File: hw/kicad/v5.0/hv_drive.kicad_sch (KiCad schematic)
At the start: 27 parts, among them P6 CONN_01X02, P8 CONN_01X03, U12 IKCM30F60GAXKMA1

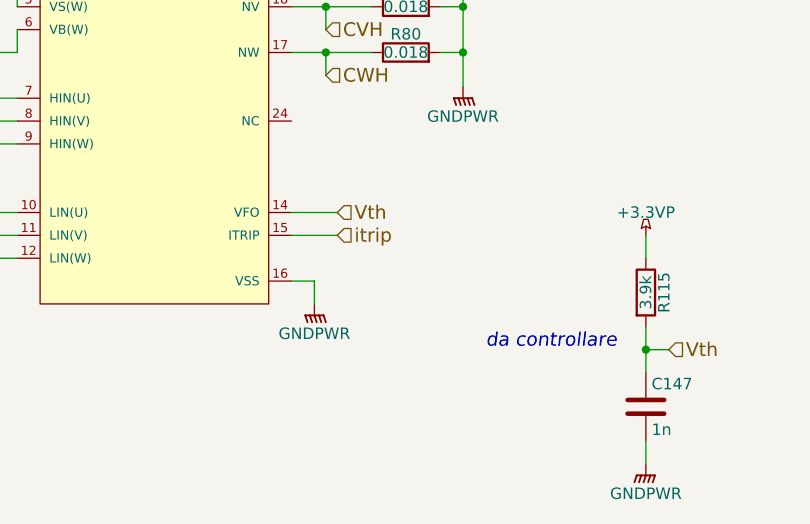
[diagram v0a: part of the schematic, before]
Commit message: add bypass cap for itrip
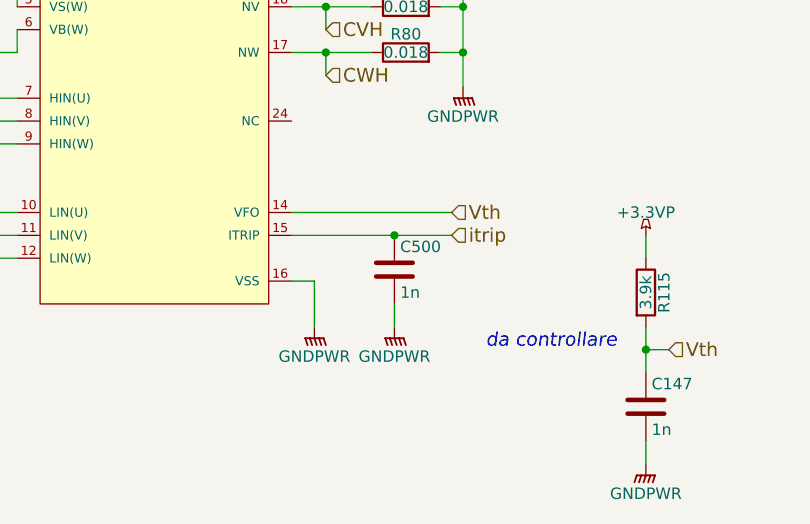
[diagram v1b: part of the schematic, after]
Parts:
- added C500: 1n, stmbl:C_0603, symbol stmbl:C
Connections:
- net GNDPWR: now also C500.2
- net itrip: now also C500.1
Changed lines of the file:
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@@
 	)
 	(junction
+		(at 163.83 120.65)
+		(diameter 0)
+		(color 0 0 0 0)
+	)
+	(junction
 		(at 104.14 118.11)
 		(diameter 0)
@@
 	(wire
 		(pts
-			(xy 154.94 128.27) (xy 154.94 125.73)
+			(xy 154.94 130.81) (xy 154.94 125.73)
 		)
 		(stroke
@@
 	(wire
 		(pts
-			(xy 152.4 118.11) (xy 157.48 118.11)
+			(xy 152.4 118.11) (xy 170.18 118.11)
 		)
 		(stroke
@@
 	(wire
 		(pts
+			(xy 163.83 120.65) (xy 170.18 120.65)
+		)
+		(stroke
+			(width 0)
+			(type default)
+		)
+	)
+	(wire
+		(pts
 			(xy 114.3 139.7) (xy 114.3 138.43)
 		)
@@
 	(wire
 		(pts
-			(xy 152.4 120.65) (xy 157.48 120.65)
+			(xy 152.4 120.65) (xy 163.83 120.65)
+		)
+		(stroke
+			(width 0)
+			(type default)
+		)
+	)
+	(wire
+		(pts
+			(xy 163.83 128.27) (xy 163.83 130.81)
 		)
 		(stroke
@@
 	(hierarchical_label "Vth"
 		(shape input)
-		(at 157.48 118.11 0)
+		(at 170.18 118.11 0)
 		(fields_autoplaced yes)
 		(effects
@@
 	(hierarchical_label "itrip"
 		(shape input)
-		(at 157.48 120.65 0)
+		(at 170.18 120.65 0)
 		(fields_autoplaced yes)
 		(effects
@@
 	(symbol
 		(lib_id "stmbl:GNDPWR")
-		(at 154.94 128.27 0)
+		(at 154.94 130.81 0)
 		(mirror y)
 		(unit 1)
@@
 		(dnp no)
 		(property "Reference" "#PWR0231"
-			(at 154.94 133.35 0)
+			(at 154.94 135.89 0)
 			(effects
 				(font
@@
 		)
 		(property "Value" "GNDPWR"
-			(at 154.94 131.572 0)
+			(at 154.94 134.112 0)
 			(effects
 				(font
@@
 		)
 		(property "Footprint" ""
-			(at 154.94 129.54 0)
+			(at 154.94 132.08 0)
 			(effects
 				(font
@@
 		)
 		(property "Datasheet" ""
-			(at 154.94 129.54 0)
+			(at 154.94 132.08 0)
 			(effects
 				(font
@@
 		)
 		(property "Description" ""
-			(at 154.94 128.27 0)
+			(at 154.94 130.81 0)
 			(effects
 				(font
@@
 	(symbol
 		(lib_id "stmbl:C")
+		(at 163.83 124.46 0)
+		(unit 1)
+		(exclude_from_sim no)
+		(in_bom yes)
+		(on_board yes)
+		(dnp no)
+		(property "Reference" "C500"
+			(at 164.465 121.92 0)
+			(effects
+				(font
+					(size 1.27 1.27)
+				)
+				(justify left)
+			)
+		)
+		(property "Value" "1n"
+			(at 164.465 127 0)
+			(effects
+				(font
+					(size 1.27 1.27)
+				)
+				(justify left)
+			)
+		)
+		(property "Footprint" "stmbl:C_0603"
+			(at 164.7952 128.27 0)
+			(effects
+				(font
+					(size 0.762 0.762)
+				)
+				(hide yes)
+			)
+		)
+		(property "Datasheet" ""
+			(at 163.83 124.46 0)
+			(effects
+				(font
+					(size 1.524 1.524)
+				)
+			)
+		)
+		(property "Description" ""
+			(at -59.69 248.92 0)
+			(effects
+				(font
+					(size 1.27 1.27)
+				)
+				(hide yes)
+			)
+		)
+		(property "InternalName" ""
+			(at 163.83 124.46 0)
+			(effects
+				(font
+					(size 1.524 1.524)
+				)
+				(hide yes)
+			)
+		)
+		(property "Manufacturer No" ""
+			(at 163.83 124.46 0)
+			(effects
+				(font
+					(size 1.524 1.524)
+				)
+				(hide yes)
+			)
+		)
+		(property "Voltage" "50V"
+			(at 163.83 124.46 0)
+			(effects
+				(font
+					(size 1.524 1.524)
+				)
+				(hide yes)
+			)
+		)
+		(property "Source" ""
+			(at 163.83 124.46 0)
+			(effects
+				(font
+					(size 1.524 1.524)
+				)
+				(hide yes)
+			)
+		)
+		(property "Tolerance" "X5R"
+			(at 163.83 124.46 0)
+			(effects
+				(font
+					(size 1.524 1.524)
+				)
+				(hide yes)
+			)
+		)
+		(property "Manufacturer" ""
+			(at -59.69 248.92 0)
+			(effects
+				(font
+					(size 1.27 1.27)
+				)
+				(hide yes)
+			)
+		)
+		(pin "1"
+		)
+		(pin "2"
+		)
+		(instances
+			(project "stmbl_4.0"
+				(path "/5befea65-3ab0-4243-80dd-808f406930a5/00000000-0000-0000-0000-00005659094d/00000000-0000-0000-0000-000056590a75"
+					(reference "C500")
+					(unit 1)
+				)
+			)
+		)
+	)
+	(symbol
+		(lib_id "stmbl:C")
 		(at 88.9 133.35 0)
 		(unit 1)
@@
 					(unit 1)
 				)
+			)
+		)
+	)
+	(symbol
+		(lib_id "stmbl:GNDPWR")
+		(at 163.83 130.81 0)
+		(mirror y)
+		(unit 1)
+		(exclude_from_sim no)
+		(in_bom yes)
+		(on_board yes)
+		(dnp no)
+		(property "Reference" "#PWR070"
+			(at 163.83 135.89 0)
+			(effects
+				(font
+					(size 1.27 1.27)
+				)
+				(hide yes)
+			)
+		)
+		(property "Value" "GNDPWR"
+			(at 163.83 134.112 0)
+			(effects
+				(font
+					(size 1.27 1.27)
+				)
+			)
+		)
+		(property "Footprint" ""
+			(at 163.83 132.08 0)
+			(effects
+				(font
+					(size 1.524 1.524)
+				)
+			)
+		)
+		(property "Datasheet" ""
+			(at 163.83 132.08 0)
+			(effects
+				(font
+					(size 1.524 1.524)
+				)
+			)
+		)
+		(property "Description" ""
+			(at 163.83 130.81 0)
+			(effects
+				(font
+					(size 1.27 1.27)
+				)
+				(hide yes)
+			)
+		)
+		(pin "1"
+		)
+		(instances
+			(project "stmbl_4.0"
+				(path "/5befea65-3ab0-4243-80dd-808f406930a5/00000000-0000-0000-0000-00005659094d/00000000-0000-0000-0000-000056590a75"
+					(reference "#PWR070")
+					(unit 1)
+				)

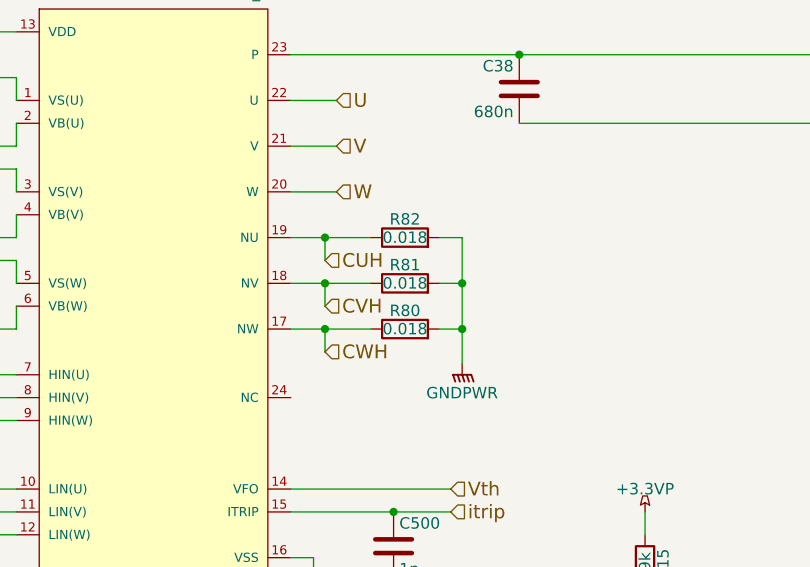
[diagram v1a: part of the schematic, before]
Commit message: change shunt value to 2 mohm
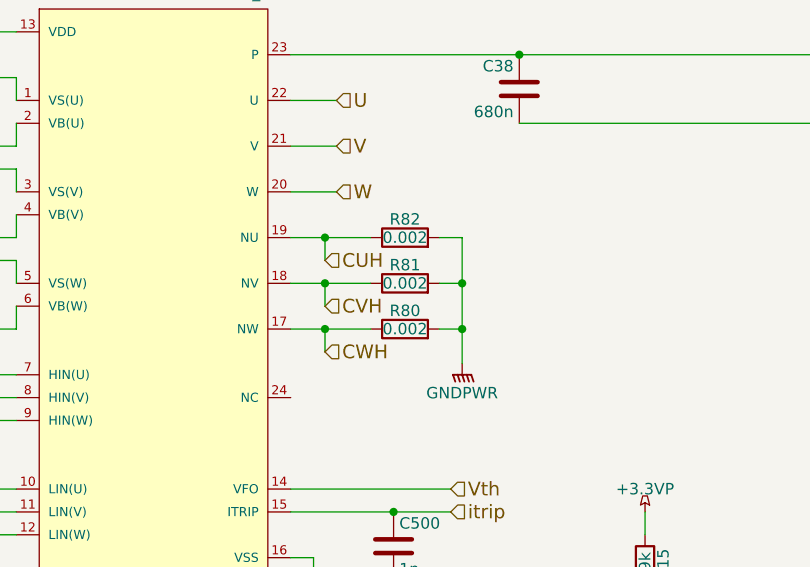
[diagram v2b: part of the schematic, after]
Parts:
- R80, R81, R82: value 0.018 -> 0.002
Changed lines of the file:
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@@
 			)
 		)
-		(property "Value" "0.018"
+		(property "Value" "0.002"
 			(at 165.1 100.33 90)
 			(effects
@@
 			)
 		)
-		(property "Value" "0.018"
+		(property "Value" "0.002"
 			(at 165.1 95.25 90)
 			(effects
@@
 			)
 		)
-		(property "Value" "0.018"
+		(property "Value" "0.002"
 			(at 165.1 90.17 90)
 			(effects

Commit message: update gerber files
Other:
- note removed: "da controllare"
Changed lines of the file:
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@@
-		)
-	)
-	(text "da controllare"
-		(exclude_from_sim no)
-		(at 173.99 133.35 0)
-		(effects
-			(font
-				(size 1.524 1.524)
-				(italic yes)
-			)
-			(justify left bottom)
 		)
 	)
